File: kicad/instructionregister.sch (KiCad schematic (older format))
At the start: 11 parts, among them U15 74LS173, U16 74LS173, U17 74LS245

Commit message: Update to current kicad libraries
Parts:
- removed D22, D23, D24, D25, D26, D27, D28, D29: LED, LEDs:LED-5MM, symbol LED
- removed U15, U16: 74LS173, Housings_DIP:DIP-16_W7.62mm_LongPads, symbol 74LS173
- removed U17: 74LS245, Housings_DIP:DIP-20_W7.62mm_LongPads, symbol 74LS245
- added D38, D39, D40, D41, D42, D43, D44, D45: LED, symbol Device:LED
- added U42: 74LS245, symbol 74xx:74LS245
- added U43, U44: 74LS173, symbol 74xx:74LS173
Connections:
- net labels removed: ~RENABLE
- wire segments 74 -> 85

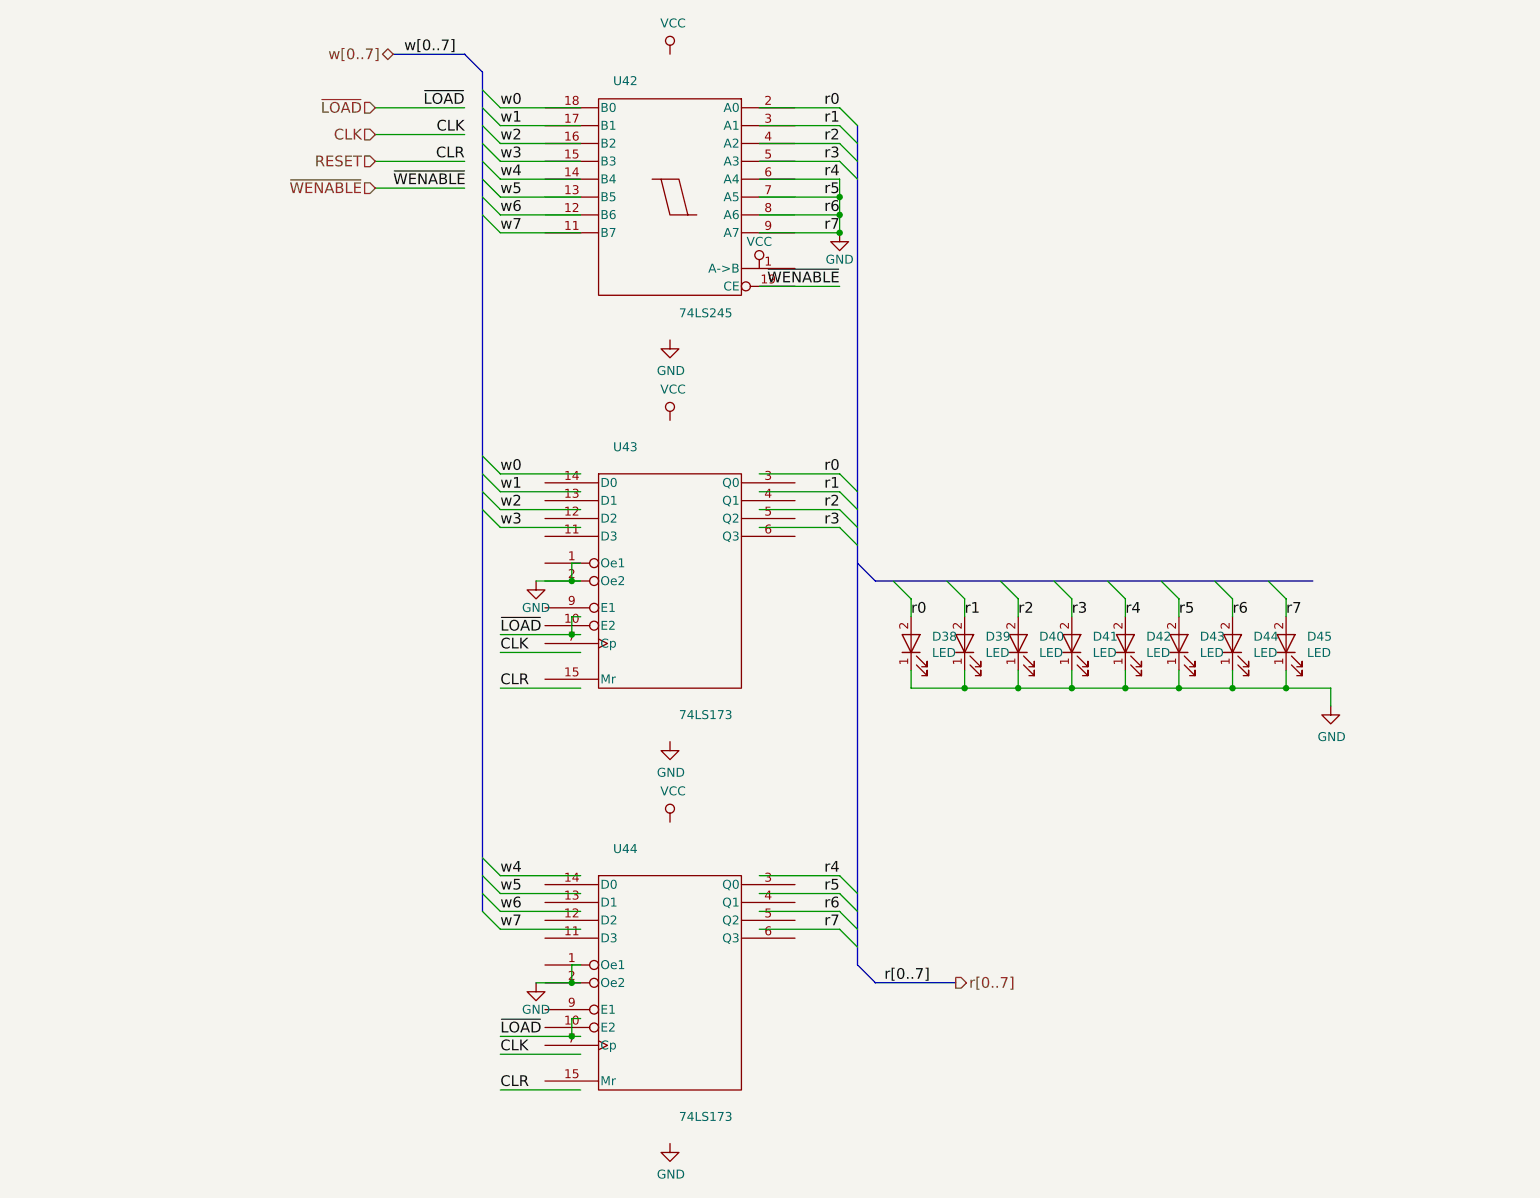
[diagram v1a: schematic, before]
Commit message: update bus names and improve sheet text
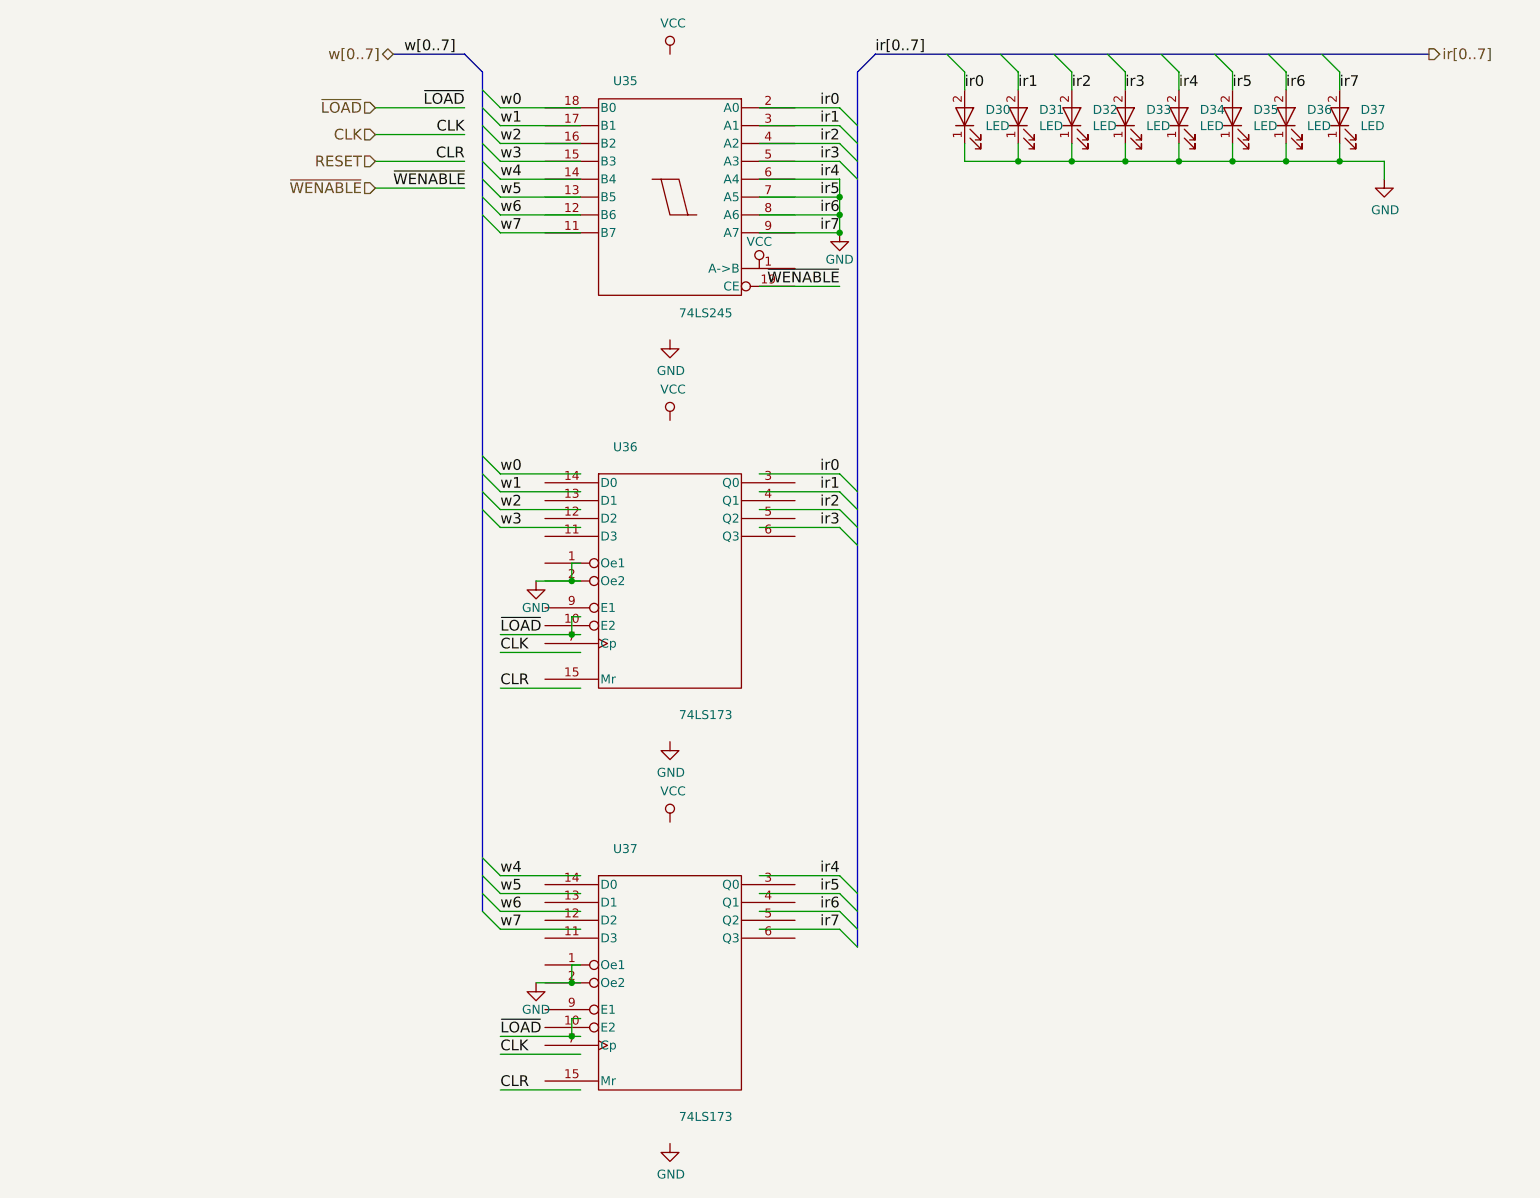
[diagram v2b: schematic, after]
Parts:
- renumbered D38 to D30, D39 to D31, D40 to D32, D41 to D33, D42 to D34, D43 to D35, D44 to D36, D45 to D37, U42 to U35, U43 to U36, U44 to U37
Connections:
- net labels added: ir0, ir1, ir2, ir3, ir4, ir5, ir6, ir7, ir[0..7]
- net labels removed: r0, r1, r2, r3, r4, r5, r6, r7, r[0..7]
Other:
- moved on the sheet: D30, D31, D32, D33, D34, D35, D36, D37
